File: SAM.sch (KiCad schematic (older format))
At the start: 61 parts, among them J301 CONN_02x05, 0.05\", SW301 Switch_DPST, SW302 Switch_DPST, U301 ATSAMD21J18A-MUT, U302 AAT4610, U303 AAT4610, X301 FC-135

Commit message: passes drc except for qfn footprint...
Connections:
- wire segments 240 -> 204
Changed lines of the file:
@@
 Connection ~ 4900 2400
 Wire Wire Line
-	4900 2400 4900 3200
-Wire Wire Line
-	4900 3200 4900 4600
+	4900 2400 4900 4600
 Connection ~ 5300 3000
 Connection ~ 5300 2400
@@
 Connection ~ 5400 2400
 Wire Wire Line
-	5400 2400 5400 2900
-Wire Wire Line
-	5400 2900 5400 4600
+	5400 2400 5400 4600
 Wire Wire Line
 	4600 2400 4600 2250
@@
 	5300 3000 3300 3000
 Wire Wire Line
-	5300 2400 5300 3000
-Wire Wire Line
-	5300 3000 5300 4600
+	5300 2400 5300 4600
 Wire Wire Line
 	5100 3100 5100 4600
@@
 	4100 3200 4100 3300
 Wire Wire Line
-	4100 3200 4500 3200
-Wire Wire Line
-	4500 3200 4900 3200
+	4100 3200 4900 3200
 Connection ~ 5700 3200
 Connection ~ 6100 3200
 Wire Wire Line
-	6500 3050 6500 3200
-Wire Wire Line
-	6500 3200 6500 3300
+	6500 3050 6500 3300
 Wire Wire Line
 	6100 3200 6100 3300
 Wire Wire Line
-	5700 3200 6100 3200
-Wire Wire Line
-	6100 3200 6500 3200
-Wire Wire Line
-	5700 3100 5700 3200
-Wire Wire Line
-	5700 3200 5700 4600
+	5700 3200 6500 3200
+Wire Wire Line
+	5700 3100 5700 4600
 Wire Wire Line
 	1800 9400 1800 9450
@@
 	1800 8700 2100 8700
 Wire Wire Line
-	1800 8100 1800 8700
-Wire Wire Line
-	1800 8700 1800 8800
+	1800 8100 1800 8800
 Wire Wire Line
 	6700 7500 8000 7500
@@
 	6700 5500 8000 5500
 Wire Wire Line
-	2700 8700 3000 8700
-Wire Wire Line
-	3000 8700 3900 8700
+	2700 8700 3900 8700
 Wire Wire Line
 	1800 8100 3900 8100
@@
 	3900 5200 2800 5200
 Wire Wire Line
-	4600 2400 4900 2400
-Wire Wire Line
-	4900 2400 5300 2400
-Wire Wire Line
-	5300 2400 5400 2400
-Wire Wire Line
-	5400 2400 5500 2400
-Wire Wire Line
-	5500 2400 5700 2400
+	4600 2400 5700 2400
 Wire Wire Line
 	4500 3300 4500 3200
 Connection ~ 4500 3200
 Wire Wire Line
-	4900 9100 4900 9200
-Wire Wire Line
-	4900 9200 4900 9400
-Wire Wire Line
-	4900 9200 5100 9200
-Wire Wire Line
-	5100 9200 5200 9200
-Wire Wire Line
-	5200 9200 5300 9200
-Wire Wire Line
-	5300 9200 5400 9200
-Wire Wire Line
-	5400 9200 5600 9200
+	4900 9100 4900 9400
+Wire Wire Line
+	4900 9200 5600 9200
 Wire Wire Line
 	5100 9200 5100 9100
@@
 	7800 3100 7600 3100
 Wire Wire Line
-	7600 3000 7600 3100
-Wire Wire Line
-	7600 3100 7600 3500
+	7600 3000 7600 3500
 Wire Wire Line
 	7800 3000 7600 3000
@@
 	2500 2800 5500 2800
 Wire Wire Line
-	5500 2400 5500 2800
-Wire Wire Line
-	5500 2800 5500 4600
+	5500 2400 5500 4600
 Connection ~ 5500 2400
 Connection ~ 5500 2800
@@
 	13800 5400 14200 5400
 Wire Wire Line
-	13800 4300 13800 5400
-Wire Wire Line
-	13800 5400 13800 7100
-Wire Wire Line
-	12500 5500 13500 5500
-Wire Wire Line
-	13500 5500 14200 5500
+	13800 4300 13800 7100
+Wire Wire Line
+	12500 5500 14200 5500
 Wire Wire Line
 	13500 5700 13500 5500
@@
 	13000 4300 13000 4400
 Wire Wire Line
-	12800 4300 13000 4300
-Wire Wire Line
-	13000 4300 13400 4300
-Wire Wire Line
-	13400 4300 13800 4300
+	12800 4300 13800 4300
 Connection ~ 13400 4300
 Connection ~ 13000 4300
@@
 	13800 7100 14200 7100
 Wire Wire Line
-	12500 7200 13500 7200
-Wire Wire Line
-	13500 7200 14200 7200
+	12500 7200 14200 7200
 Wire Wire Line
 	13500 7400 13500 7200
@@
 	11400 1600 11400 1700
 Wire Wire Line
-	10700 2400 11000 2400
-Wire Wire Line
-	11000 2400 11300 2400
-Wire Wire Line
-	11300 2400 11400 2400
-Wire Wire Line
-	11400 2400 12600 2400
+	10700 2400 12600 2400
 Wire Wire Line
 	11400 2400 11400 2300
@@
 	10100 2800 10000 2800
 Wire Wire Line
-	10000 2400 10000 2800
-Wire Wire Line
-	10000 2800 10000 3200
+	10000 2400 10000 3200
 $Comp
 L Switch_DPST SW301
@@
 	14700 1600 14700 1700
 Wire Wire Line
-	14000 2400 14300 2400
-Wire Wire Line
-	14300 2400 14600 2400
-Wire Wire Line
-	14600 2400 14700 2400
-Wire Wire Line
-	14700 2400 15600 2400
+	14000 2400 15600 2400
 Wire Wire Line
 	14700 2400 14700 2300
@@
 	13400 2800 13300 2800
 Wire Wire Line
-	13300 2400 13300 2800
-Wire Wire Line
-	13300 2800 13300 3200
+	13300 2400 13300 3200
 $Comp
 L Switch_DPST SW302
@@
 	8900 3800 8700 3800
 Wire Wire Line
-	8700 3800 8700 4000
-Wire Wire Line
-	8700 4000 8700 4200
-Wire Wire Line
-	8700 4200 8700 4400
-Wire Wire Line
-	8700 4400 8700 4600
+	8700 3800 8700 4600
 Wire Wire Line
 	8900 4400 8700 4400

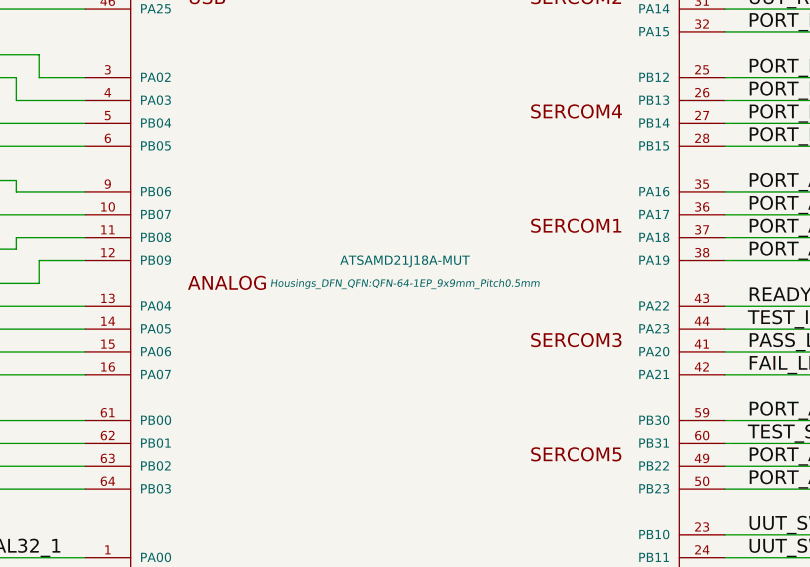
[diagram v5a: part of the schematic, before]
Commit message: qfn swapped, another mount hole added, passes drc
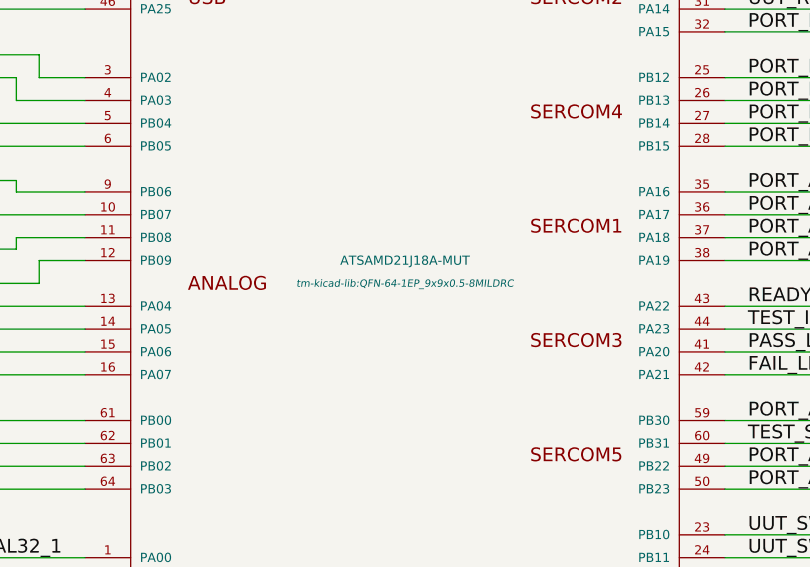
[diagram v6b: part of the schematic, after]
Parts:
- U301: footprint Housings_DFN_QFN:QFN-64-1EP_9x9mm_Pitch0.5mm -> tm-kicad-lib:QFN-64-1EP_9x9x0.5-8MILDRC
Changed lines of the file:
@@
 F 0 "U301" H 4200 8850 40  0000 C CNN
 F 1 "ATSAMD21J18A-MUT" H 5300 6800 40  0000 C CNN
-F 2 "Housings_DFN_QFN:QFN-64-1EP_9x9mm_Pitch0.5mm" H 5300 6700 32  0000 C CIN
+F 2 "tm-kicad-lib:QFN-64-1EP_9x9x0.5-8MILDRC" H 5300 6700 32  0000 C CIN
 F 3 "" H 4100 6450 60  0000 C CNN
 	1    5300 6800
